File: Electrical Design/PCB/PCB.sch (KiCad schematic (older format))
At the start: 57 parts, among them J1 Conn_02x03_Odd_Even, J2 10118193-0001LF, M1 Camera_Servo, M2 Release_Servo, Q1 LED_MOS, Q2 CAMERA_MOS, Q3 RELEASE_MOS, Q4 BUZZER_MOS, U1 ADP3338AKCZ-5-R7, U2 BNO080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

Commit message: Generated initial PCB from schematic
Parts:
- D5: symbol dk_Diodes-Rectifiers-Single:1N4148W-TP -> PCB-rescue:1N4148W-TP-dk_Diodes-Rectifiers-Single
- J2: symbol dk_USB-DVI-HDMI-Connectors:10118193-0001LF -> PCB-rescue:10118193-0001LF-dk_USB-DVI-HDMI-Connectors
- LS1: symbol CSS-95B30-SMT:CSS-95B30-SMT -> PCB-rescue:CSS-95B30-SMT-CSS-95B30-SMT
- MOD1: symbol dk_RF-Transceiver-Modules:XBP9B-DMWT-002 -> PCB-rescue:XBP9B-DMWT-002-dk_RF-Transceiver-Modules
- Q1, Q2, Q3, Q4: symbol dk_Transistors-FETs-MOSFETs-Single:2N7002K-T1-E3 -> PCB-rescue:2N7002K-T1-E3-dk_Transistors-FETs-MOSFETs-Single
- U1, U3: symbol ADP3338AKCZ-5-R7:ADP3338AKCZ-5-R7 -> PCB-rescue:ADP3338AKCZ-5-R7-ADP3338AKCZ-5-R7
- U2: symbol BNO080:BNO080 -> PCB-rescue:BNO080-BNO080
- U4: symbol dk_Clock-Timing-Real-Time-Clocks:PCF8523T_1_118 -> PCB-rescue:PCF8523T_1_118-dk_Clock-Timing-Real-Time-Clocks
- U5: symbol MS560702BA03-50:MS560702BA03-50 -> PCB-rescue:MS560702BA03-50-MS560702BA03-50
- U6: symbol SS495A:SS495A -> PCB-rescue:SS495A-SS495A
- U7: symbol Skyfire_Custom_Components:Adafruit_746 -> PCB-rescue:Adafruit_746-Skyfire_Custom_Components
- U8: symbol Skyfire_Custom_Components:Openlog -> PCB-rescue:Openlog-Skyfire_Custom_Components
- U9: symbol MCU_Microchip_ATmega:ATxmega128A4U-AU -> PCB-rescue:ATxmega128A4U-AU-MCU_Microchip_ATmega
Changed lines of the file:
@@
 $EndDescr
 $Comp
-L MCU_Microchip_ATmega:ATxmega128A4U-AU U9
+L PCB-rescue:ATxmega128A4U-AU-MCU_Microchip_ATmega U9
 U 1 1 5C4816FD
 P 9650 4650
@@
 PDI_CLK
 $Comp
-L MS560702BA03-50:MS560702BA03-50 U5
+L PCB-rescue:MS560702BA03-50-MS560702BA03-50 U5
 U 1 1 5C48EC0D
 P 4750 5750
@@
 ~SS_5607
 $Comp
-L BNO080:BNO080 U2
+L PCB-rescue:BNO080-BNO080 U2
 U 1 1 5C492D9E
 P 1950 2100
@@
 PA6-Therm
 $Comp
-L ADP3338AKCZ-5-R7:ADP3338AKCZ-5-R7 U1
+L PCB-rescue:ADP3338AKCZ-5-R7-ADP3338AKCZ-5-R7 U1
 U 1 1 5C4D6E8B
 P 1750 5700
@@
 	900  5700 1050 5700
 $Comp
-L ADP3338AKCZ-5-R7:ADP3338AKCZ-5-R7 U3
+L PCB-rescue:ADP3338AKCZ-5-R7-ADP3338AKCZ-5-R7 U3
 U 1 1 5C4ECC23
 P 3450 6900
@@
 Connection ~ 1050 750
 $Comp
-L SS495A:SS495A U6
+L PCB-rescue:SS495A-SS495A U6
 U 1 1 5C4FD36A
 P 5600 6900
@@
 $EndComp
 $Comp
-L dk_Clock-Timing-Real-Time-Clocks:PCF8523T_1_118 U4
+L PCB-rescue:PCF8523T_1_118-dk_Clock-Timing-Real-Time-Clocks U4
 U 1 1 5C4D622C
 P 4750 3900
@@
 	5100 7550 5100 6500
 $Comp
-L dk_RF-Transceiver-Modules:XBP9B-DMWT-002 MOD1
+L PCB-rescue:XBP9B-DMWT-002-dk_RF-Transceiver-Modules MOD1
 U 1 1 5C555561
 P 4800 2300
@@
 PA5-Hall_Effect
 $Comp
-L Skyfire_Custom_Components:Adafruit_746 U7
+L PCB-rescue:Adafruit_746-Skyfire_Custom_Components U7
 U 1 1 5C5FC17D
 P 7450 1350
@@
 	6350 800  6500 800
 $Comp
-L Skyfire_Custom_Components:Openlog U8
+L PCB-rescue:Openlog-Skyfire_Custom_Components U8
 U 1 1 5C61ADA8
 P 7300 2000
@@
 $EndComp
 $Comp
-L dk_Transistors-FETs-MOSFETs-Single:2N7002K-T1-E3 Q1
+L PCB-rescue:2N7002K-T1-E3-dk_Transistors-FETs-MOSFETs-Single Q1
 U 1 1 5C64B586
 P 6400 3200
@@
 Release_Servo
 $Comp
-L dk_Transistors-FETs-MOSFETs-Single:2N7002K-T1-E3 Q3
+L PCB-rescue:2N7002K-T1-E3-dk_Transistors-FETs-MOSFETs-Single Q3
 U 1 1 5C72FE6D
 P 8300 2650
@@
 	8500 1350 8500 1550
 $Comp
-L dk_Transistors-FETs-MOSFETs-Single:2N7002K-T1-E3 Q2
+L PCB-rescue:2N7002K-T1-E3-dk_Transistors-FETs-MOSFETs-Single Q2
 U 1 1 5C72F9D1
 P 8300 1550
@@
 	8950 1350 8500 1350
 $Comp
-L dk_USB-DVI-HDMI-Connectors:10118193-0001LF J2
+L PCB-rescue:10118193-0001LF-dk_USB-DVI-HDMI-Connectors J2
 U 1 1 5C83D693
 P 12500 1600
@@
 	13000 1400 12800 1400
 $Comp
-L dk_Diodes-Rectifiers-Single:1N4148W-TP D5
+L PCB-rescue:1N4148W-TP-dk_Diodes-Rectifiers-Single D5
 U 1 1 5C88A6D8
 P 13200 1400
@@
 Connection ~ 10950 5050
 $Comp
-L CSS-95B30-SMT:CSS-95B30-SMT LS1
+L PCB-rescue:CSS-95B30-SMT-CSS-95B30-SMT LS1
 U 1 1 5C6232EA
 P 13300 4000
@@
 $EndComp
 $Comp
-L dk_Transistors-FETs-MOSFETs-Single:2N7002K-T1-E3 Q4
+L PCB-rescue:2N7002K-T1-E3-dk_Transistors-FETs-MOSFETs-Single Q4
 U 1 1 5C623A5F
 P 12500 4000

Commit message: Update Thermistor Footprint
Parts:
- TH1: footprint Resistor_THT:R_Axial_Power_L48.0mm_W12.5mm_P55.88mm -> Capacitor_THT:CP_Radial_D4.0mm_P1.50mm
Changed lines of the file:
@@
 F 0 "TH1" V 810 6950 50  0000 C CNN
 F 1 "NTCLE100" V 901 6950 50  0000 C CNN
-F 2 "Resistor_THT:R_Axial_Power_L48.0mm_W12.5mm_P55.88mm" H 1100 7000 50  0001 C CNN
+F 2 "Capacitor_THT:CP_Radial_D4.0mm_P1.50mm" H 1100 7000 50  0001 C CNN
 F 3 "~" H 1100 7000 50  0001 C CNN
 	1    1100 6950

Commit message: Batteries and Camera
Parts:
- added U10: Adafruit_Cam, Connectors:MOLEX-1X3, symbol Skyfire_Custom_Components:Adafruit_Cam
- added U11, U12: BH123A, BH123A:BH123A, symbol BH123A:BH123A
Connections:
- net +5V: now also U10.1 (Vin)
- net +6V: now also U11.+
- net GND: now also U10.2 (GND), U12.-
- net CAMERA_DATA: now reaches U9.43 (PA3)
- net CAMERA_DATA: now also U10.3 (DATA)
- new net: U11.-, U12.+
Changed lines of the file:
@@
 NoConn ~ 6500 1000
 NoConn ~ 6500 1100
+$Comp
+L power:GND #PWR0101
+U 1 1 5C5D4CBC
+P -1400 4450
+F 0 "#PWR0101" H -1400 4200 50  0001 C CNN
+F 1 "GND" H -1395 4277 50  0000 C CNN
+F 2 "" H -1400 4450 50  0001 C CNN
+F 3 "" H -1400 4450 50  0001 C CNN
+	1    -1400 4450
+	1    0    0    -1
+$EndComp
+$Comp
+L power:+6V #PWR0102
+U 1 1 5C5DD946
+P -1400 3650
+F 0 "#PWR0102" H -1400 3500 50  0001 C CNN
+F 1 "+6V" H -1385 3823 50  0000 C CNN
+F 2 "" H -1400 3650 50  0001 C CNN
+F 3 "" H -1400 3650 50  0001 C CNN
+	1    -1400 3650
+	1    0    0    -1
+$EndComp
+$Comp
+L Skyfire_Custom_Components:Adafruit_Cam U10
+U 1 1 5C5F2365
+P -1350 2200
+F 0 "U10" H -1172 2115 50  0000 L CNN
+F 1 "Adafruit_Cam" H -1172 2024 50  0000 L CNN
+F 2 "Connectors:MOLEX-1X3" H -1350 2200 50  0001 C CNN
+F 3 "" H -1350 2200 50  0001 C CNN
+	1    -1350 2200
+	1    0    0    -1
+$EndComp
+$Comp
+L power:+5V #PWR0103
+U 1 1 5C5F2C9E
+P -1550 2500
+F 0 "#PWR0103" H -1550 2350 50  0001 C CNN
+F 1 "+5V" H -1535 2673 50  0000 C CNN
+F 2 "" H -1550 2500 50  0001 C CNN
+F 3 "" H -1550 2500 50  0001 C CNN
+	1    -1550 2500
+	-1   0    0    1
+$EndComp
+$Comp
+L power:GND #PWR0104
+U 1 1 5C5F3219
+P -1400 2500
+F 0 "#PWR0104" H -1400 2250 50  0001 C CNN
+F 1 "GND" H -1395 2327 50  0000 C CNN
+F 2 "" H -1400 2500 50  0001 C CNN
+F 3 "" H -1400 2500 50  0001 C CNN
+	1    -1400 2500
+	1    0    0    -1
+$EndComp
+Text Label 10350 3850 0    50   ~ 0
+CAMERA_DATA
+Text Label -1250 2500 3    50   ~ 0
+CAMERA_DATA
+$Comp
+L BH123A:BH123A U12
+U 1 1 5C61998B
+P -1400 4250
+F 0 "U12" V -1354 4117 50  0000 R CNN
+F 1 "BH123A" V -1445 4117 50  0000 R CNN
+F 2 "BH123A:BH123A" H -1400 4250 50  0001 L BNN
+F 3 "Unavailable" H -1400 4250 50  0001 L BNN
+F 4 "Batt Holder Cr123a Thru Hole" H -1400 4250 50  0001 L BNN "Field4"
+F 5 "None" H -1400 4250 50  0001 L BNN "Field5"
+F 6 "MPD _Memory" H -1400 4250 50  0001 L BNN "Field6"
+F 7 "None" H -1400 4250 50  0001 L BNN "Field7"
+F 8 "BH123A" H -1400 4250 50  0001 L BNN "Field8"
+	1    -1400 4250
+	0    -1   -1   0
+$EndComp
+$Comp
+L BH123A:BH123A U11
+U 1 1 5C62AE2B
+P -1400 3850
+F 0 "U11" V -1354 3717 50  0000 R CNN
+F 1 "BH123A" V -1445 3717 50  0000 R CNN
+F 2 "BH123A:BH123A" H -1400 3850 50  0001 L BNN
+F 3 "Unavailable" H -1400 3850 50  0001 L BNN
+F 4 "Batt Holder Cr123a Thru Hole" H -1400 3850 50  0001 L BNN "Field4"
+F 5 "None" H -1400 3850 50  0001 L BNN "Field5"
+F 6 "MPD _Memory" H -1400 3850 50  0001 L BNN "Field6"
+F 7 "None" H -1400 3850 50  0001 L BNN "Field7"
+F 8 "BH123A" H -1400 3850 50  0001 L BNN "Field8"
+	1    -1400 3850
+	0    -1   -1   0
+$EndComp
 $EndSCHEMATC

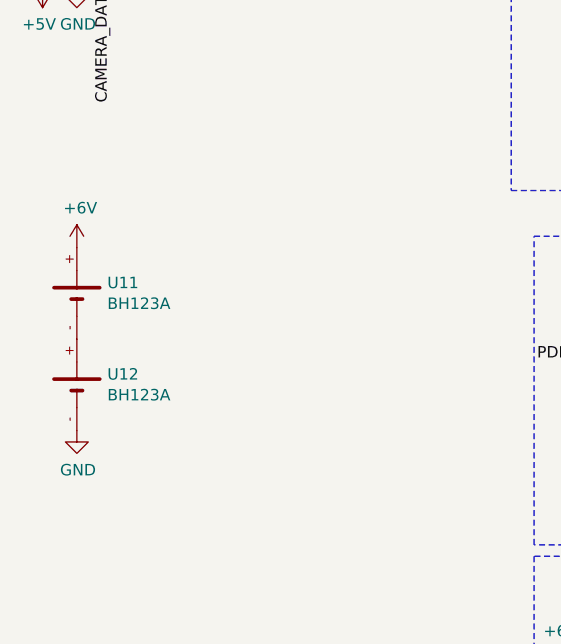
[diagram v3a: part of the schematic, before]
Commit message: Fix Batteries
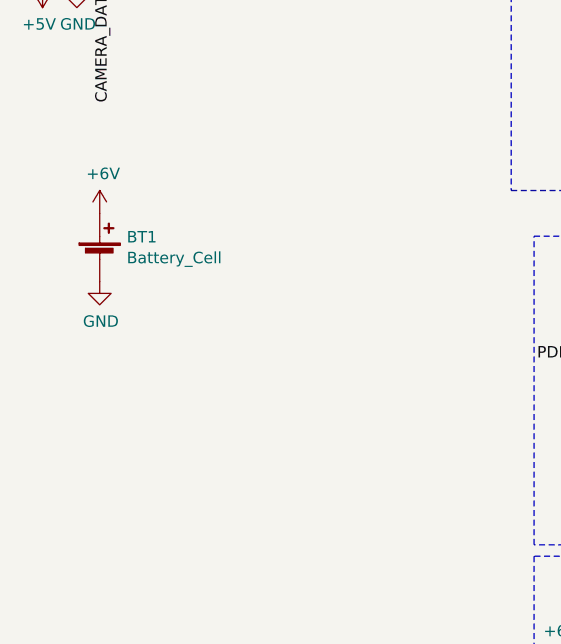
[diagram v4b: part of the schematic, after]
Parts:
- removed U11, U12: BH123A, BH123A:BH123A, symbol BH123A:BH123A
- added BT1: Battery_Cell, Connectors:MOLEX-1X2, symbol Device:Battery_Cell
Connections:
- net +6V: now also BT1.1 (+)
- net GND: now also BT1.2 (-)
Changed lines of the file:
@@
 L power:GND #PWR0101
 U 1 1 5C5D4CBC
-P -1400 4450
-F 0 "#PWR0101" H -1400 4200 50  0001 C CNN
-F 1 "GND" H -1395 4277 50  0000 C CNN
-F 2 "" H -1400 4450 50  0001 C CNN
-F 3 "" H -1400 4450 50  0001 C CNN
-	1    -1400 4450
+P -1300 3800
+F 0 "#PWR0101" H -1300 3550 50  0001 C CNN
+F 1 "GND" H -1295 3627 50  0000 C CNN
+F 2 "" H -1300 3800 50  0001 C CNN
+F 3 "" H -1300 3800 50  0001 C CNN
+	1    -1300 3800
 	1    0    0    -1
 $EndComp
@@
 L power:+6V #PWR0102
 U 1 1 5C5DD946
-P -1400 3650
-F 0 "#PWR0102" H -1400 3500 50  0001 C CNN
-F 1 "+6V" H -1385 3823 50  0000 C CNN
-F 2 "" H -1400 3650 50  0001 C CNN
-F 3 "" H -1400 3650 50  0001 C CNN
-	1    -1400 3650
+P -1300 3500
+F 0 "#PWR0102" H -1300 3350 50  0001 C CNN
+F 1 "+6V" H -1285 3673 50  0000 C CNN
+F 2 "" H -1300 3500 50  0001 C CNN
+F 3 "" H -1300 3500 50  0001 C CNN
+	1    -1300 3500
 	1    0    0    -1
 $EndComp
@@
 CAMERA_DATA
 $Comp
-L BH123A:BH123A U12
-U 1 1 5C61998B
-P -1400 4250
-F 0 "U12" V -1354 4117 50  0000 R CNN
-F 1 "BH123A" V -1445 4117 50  0000 R CNN
-F 2 "BH123A:BH123A" H -1400 4250 50  0001 L BNN
-F 3 "Unavailable" H -1400 4250 50  0001 L BNN
-F 4 "Batt Holder Cr123a Thru Hole" H -1400 4250 50  0001 L BNN "Field4"
-F 5 "None" H -1400 4250 50  0001 L BNN "Field5"
-F 6 "MPD _Memory" H -1400 4250 50  0001 L BNN "Field6"
-F 7 "None" H -1400 4250 50  0001 L BNN "Field7"
-F 8 "BH123A" H -1400 4250 50  0001 L BNN "Field8"
-	1    -1400 4250
-	0    -1   -1   0
-$EndComp
-$Comp
-L BH123A:BH123A U11
-U 1 1 5C62AE2B
-P -1400 3850
-F 0 "U11" V -1354 3717 50  0000 R CNN
-F 1 "BH123A" V -1445 3717 50  0000 R CNN
-F 2 "BH123A:BH123A" H -1400 3850 50  0001 L BNN
-F 3 "Unavailable" H -1400 3850 50  0001 L BNN
-F 4 "Batt Holder Cr123a Thru Hole" H -1400 3850 50  0001 L BNN "Field4"
-F 5 "None" H -1400 3850 50  0001 L BNN "Field5"
-F 6 "MPD _Memory" H -1400 3850 50  0001 L BNN "Field6"
-F 7 "None" H -1400 3850 50  0001 L BNN "Field7"
-F 8 "BH123A" H -1400 3850 50  0001 L BNN "Field8"
-	1    -1400 3850
-	0    -1   -1   0
+L Device:Battery_Cell BT1
+U 1 1 5C5FAEB2
+P -1300 3700
+F 0 "BT1" H -1182 3796 50  0000 L CNN
+F 1 "Battery_Cell" H -1182 3705 50  0000 L CNN
+F 2 "Connectors:MOLEX-1X2" V -1300 3760 50  0001 C CNN
+F 3 "~" V -1300 3760 50  0001 C CNN
+	1    -1300 3700
+	1    0    0    -1
 $EndComp
 $EndSCHEMATC

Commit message: Fix Connector
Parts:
- J1: footprint Connector:Tag-Connect_TC2030-IDC-FP_2x03_P1.27mm_Vertical -> Connectors:2X3
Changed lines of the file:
@@
 F 0 "J1" H 1200 4600 50  0000 C CNN
 F 1 "Conn_02x03_Odd_Even" H 1200 4500 50  0000 C CNN
-F 2 "Connector:Tag-Connect_TC2030-IDC-FP_2x03_P1.27mm_Vertical" H 1150 4250 50  0001 C CNN
+F 2 "Connectors:2X3" H 1150 4250 50  0001 C CNN
 F 3 "~" H 1150 4250 50  0001 C CNN
 	1    1150 4250

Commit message: m
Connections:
- net GPS_RX is gone; now on net GPS_MOSI: U7.6 (RX)
- net GPS_TX is gone; now on net GPS_MISO: U7.5 (TX)
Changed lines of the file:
@@
 $EndComp
 Text Label 7200 800  0    50   ~ 0
-GPS_TX
+GPS_MISO
 Text Label 7200 700  0    50   ~ 0
-GPS_RX
+GPS_MOSI
 Text Label 8950 5150 2    50   ~ 0
 GPS_MISO

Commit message: a
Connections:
- net PA5-Hall_effect is gone; now on net PA5-Hall_Effect: U6.3 (OUT)
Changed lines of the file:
@@
 	5300 7200 5400 7200
 Text Label 6400 7000 0    50   ~ 0
-PA5-Hall_effect
+PA5-Hall_Effect
 $Comp
 L Device:C_Small C11

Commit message: update
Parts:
- removed R10, R11: 10k, Resistor_SMD:R_0805_2012Metric_Pad1.15x1.40mm_HandSolder, symbol Device:R_Small
- added C? (x2): 100nF, Capacitor_SMD:C_0805_2012Metric_Pad1.15x1.40mm_HandSolder, symbol Device:C_Small
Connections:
- net GND: now also C?.2, C?.2
- net MCU_VCC: now also C?.1, C?.1
- net at M2.3 (-): now also Q3.3 (D)
- net at M1.3 (-): now also Q2.3 (D)
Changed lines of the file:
@@
 L power:GND #PWR044
 U 1 1 5C4834EF
-P 7450 5950
-F 0 "#PWR044" H 7450 5700 50  0001 C CNN
-F 1 "GND" H 7455 5777 50  0000 C CNN
-F 2 "" H 7450 5950 50  0001 C CNN
-F 3 "" H 7450 5950 50  0001 C CNN
-	1    7450 5950
+P 7800 5950
+F 0 "#PWR044" H 7800 5700 50  0001 C CNN
+F 1 "GND" H 7805 5777 50  0000 C CNN
+F 2 "" H 7800 5950 50  0001 C CNN
+F 3 "" H 7800 5950 50  0001 C CNN
+	1    7800 5950
 	0    -1   -1   0
 $EndComp
@@
 	7100 5950 7300 5950
 Connection ~ 7300 5950
-Wire Wire Line
-	7300 5950 7450 5950
 Wire Wire Line
 	7100 5750 7200 5750
@@
 NoConn ~ 1450 4250
 NoConn ~ 950  4250
-Text Label 7400 5750 0    50   ~ 0
+Text Label 7750 5750 0    50   ~ 0
 MCU_VCC
-Wire Wire Line
-	7300 5750 7400 5750
 Connection ~ 7300 5750
 Text Label 9650 3250 1    50   ~ 0
@@
 	2050 450  500  450
 Wire Notes Line
-	6900 5400 6400 5400
-Wire Notes Line
-	6400 5400 6400 5900
-Wire Notes Line
-	6400 5900 6900 5900
-Wire Notes Line
-	6900 5900 6900 6300
-Wire Notes Line
-	6900 6300 7500 6300
-Wire Notes Line
-	7500 6300 7500 6100
-Wire Notes Line
-	7500 6100 7750 6100
-Wire Notes Line
-	7750 6100 7750 5750
-Wire Notes Line
-	7750 5750 8100 5750
-Wire Notes Line
-	8100 5750 8100 5100
-Wire Notes Line
-	8100 5100 7650 5100
-Wire Notes Line
-	7650 5100 7650 4800
-Wire Notes Line
-	7650 4800 6900 4800
-Wire Notes Line
-	6900 4800 6900 5400
-Wire Notes Line
 	2300 6350 2300 7200
 Wire Notes Line
@@
 Wire Notes Line
 	4100 6350 2300 6350
-Wire Notes Line
-	5100 6500 6900 6500
-Wire Notes Line
-	6900 6500 6900 7550
-Wire Notes Line
-	6900 7550 5100 7550
-Wire Notes Line
-	5100 7550 5100 6500
 $Comp
 L PCB-rescue:XBP9B-DMWT-002-dk_RF-Transceiver-Modules MOD1
@@
 RELEASE_MOS
 $Comp
-L Device:R_Small R11
-U 1 1 5C7ED981
-P 9050 2400
-F 0 "R11" V 9150 2250 50  0000 C CNN
-F 1 "10k" V 9150 2400 50  0000 C CNN
-F 2 "Resistor_SMD:R_0805_2012Metric_Pad1.15x1.40mm_HandSolder" H 9050 2400 50  0001 C CNN
-F 3 "~" H 9050 2400 50  0001 C CNN
-	1    9050 2400
-	0    -1   -1   0
-$EndComp
-$Comp
-L Device:R_Small R10
-U 1 1 5C7FD208
-P 9050 1350
-F 0 "R10" V 9150 1200 50  0000 C CNN
-F 1 "10k" V 9150 1350 50  0000 C CNN
-F 2 "Resistor_SMD:R_0805_2012Metric_Pad1.15x1.40mm_HandSolder" H 9050 1350 50  0001 C CNN
-F 3 "~" H 9050 1350 50  0001 C CNN
-	1    9050 1350
-	0    -1   -1   0
-$EndComp
-Wire Wire Line
-	10050 2400 9150 2400
-Wire Wire Line
-	8950 2400 8500 2400
-Wire Wire Line
-	10050 1350 9150 1350
-Wire Wire Line
-	8950 1350 8500 1350
-$Comp
 L PCB-rescue:10118193-0001LF-dk_USB-DVI-HDMI-Connectors J2
 U 1 1 5C83D693
@@
 	1    0    0    -1
 $EndComp
+Wire Wire Line
+	8500 1350 10050 1350
+Wire Wire Line
+	8500 2400 10050 2400
+$Comp
+L Device:C_Small C?
+U 1 1 5C6B77F9
+P 7500 5850
+F 0 "C?" V 7450 5550 50  0000 C CNN
+F 1 "100nF" V 7550 5550 50  0000 C CNN
+F 2 "Capacitor_SMD:C_0805_2012Metric_Pad1.15x1.40mm_HandSolder" H 7500 5850 50  0001 C CNN
+F 3 "~" H 7500 5850 50  0001 C CNN
+	1    7500 5850
+	1    0    0    -1
+$EndComp
+$Comp
+L Device:C_Small C?
+U 1 1 5C6B7965
+P 7700 5850
+F 0 "C?" V 7650 5550 50  0000 C CNN
+F 1 "100nF" V 7750 5550 50  0000 C CNN
+F 2 "Capacitor_SMD:C_0805_2012Metric_Pad1.15x1.40mm_HandSolder" H 7700 5850 50  0001 C CNN
+F 3 "~" H 7700 5850 50  0001 C CNN
+	1    7700 5850
+	1    0    0    -1
+$EndComp
+Wire Wire Line
+	7300 5750 7500 5750
+Connection ~ 7500 5750
+Wire Wire Line
+	7500 5750 7700 5750
+Connection ~ 7700 5750
+Wire Wire Line
+	7700 5750 7750 5750
+Wire Wire Line
+	7300 5950 7500 5950
+Connection ~ 7500 5950
+Wire Wire Line
+	7500 5950 7700 5950
+Connection ~ 7700 5950
+Wire Wire Line
+	7700 5950 7800 5950
 $EndSCHEMATC
